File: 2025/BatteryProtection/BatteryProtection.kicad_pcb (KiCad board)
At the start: 2 copper layers, 140.1 x 58.4 mm, 57 parts, among them J1 Conn_01x02_Socket, J2 Conn_01x02_Pin, J3 Conn_01x02_Pin, Q1 IXTA140P05T, Q10 BC847, Q11 BC847, Q12 BC847, Q2 BC847, Q3 BC847, Q4 BC847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

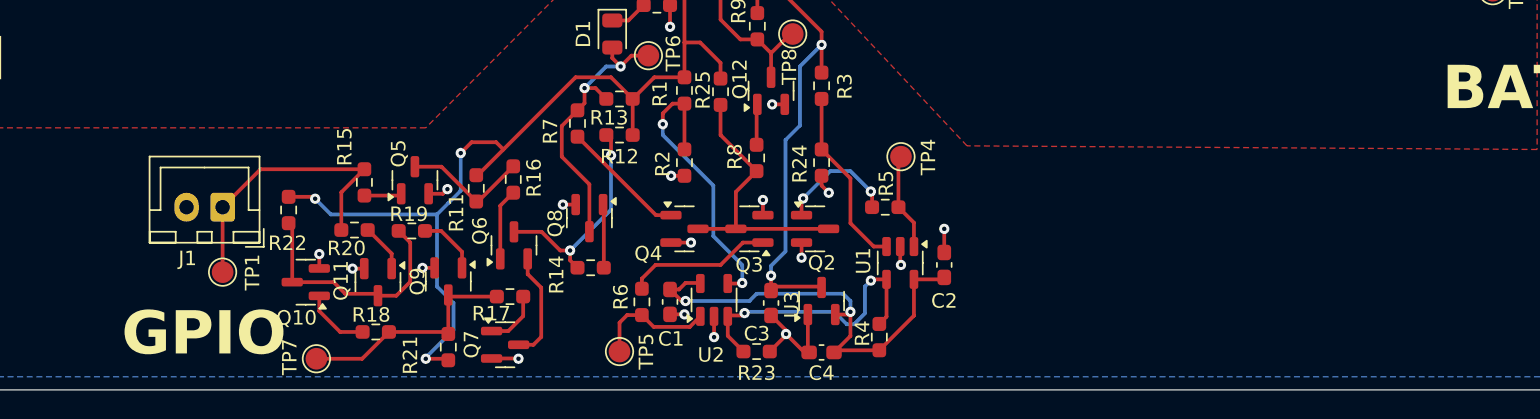
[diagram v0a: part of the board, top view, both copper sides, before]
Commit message: Added Switch to Bat Protect Board
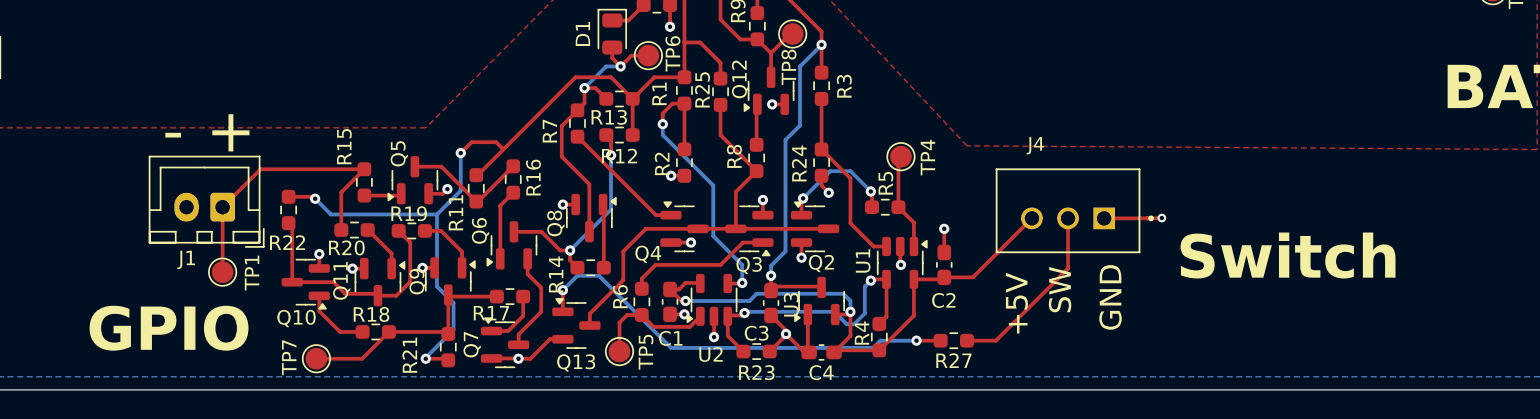
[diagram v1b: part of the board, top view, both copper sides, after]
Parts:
- added J4: Conn_01x03_Pin, B3B-XH-A:JST_B3B-XH-A, F.Cu at (222.5, 105.0)
- added Q13: BC847, Package_TO_SOT_SMD:SOT-23, F.Cu at (188.4, 113.0)
- added R27: 1M, Resistor_SMD:R_0603_1608Metric_Pad0.98x0.95mm_HandSolder, F.Cu at (214.6, 114.0)
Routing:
- net Net-(Q13-B): track 0.00 -> 30.4 mm, vias 0 -> 2
- net SW Out: track 0.00 -> 12.5 mm
- net Net-(Q13-C): track 19.3 -> 31.2 mm
- net +5V: track 32.2 -> 40.0 mm
- net GND: track 37.6 -> 45.3 mm, vias 19 -> 20
- net Net-(Q6-E): track 7.59 -> 6.99 mm
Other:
- board text added: "+"
- board text added: "+5V"
- board text added: "-"
- board text added: "GND"
- board text added: "SW"
- board text added: "Switch"
